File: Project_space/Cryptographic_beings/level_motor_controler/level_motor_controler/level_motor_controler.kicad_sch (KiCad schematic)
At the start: 7 parts, among them J1 Conn_01x15, J2 Conn_01x15, J3 Conn_01x04, J4 Conn_02x03_Odd_Even, J5 Conn_02x03_Odd_Even, J6 Conn_01x02

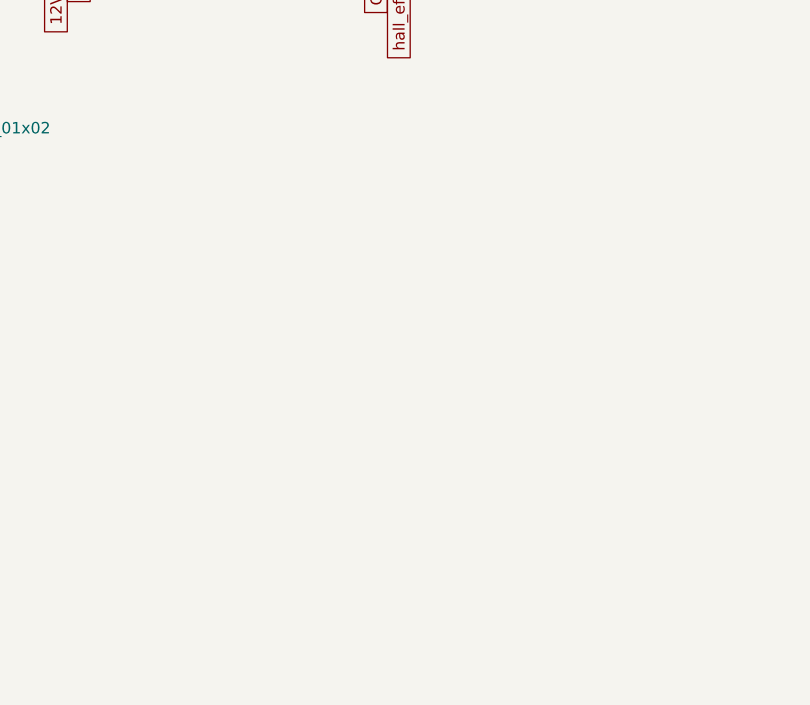
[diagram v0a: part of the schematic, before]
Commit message: Fix Nano pin mapping: swap STEP/DIR to match actual wiring (D4=DIR, D5=STP, D3=HALL)
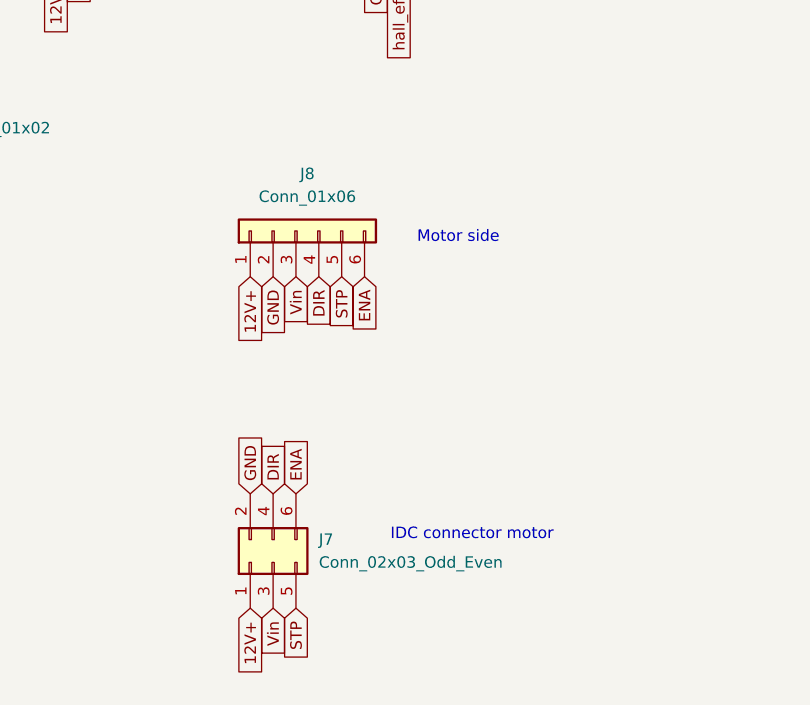
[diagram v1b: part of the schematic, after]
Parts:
- added J7: Conn_02x03_Odd_Even, symbol Connector_Generic:Conn_02x03_Odd_Even
- added J8: Conn_01x06, symbol Connector_Generic:Conn_01x06
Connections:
- net 12V+: now also J7.1 (Pin_1), J8.1 (Pin_1)
- net GND: now also J7.2 (Pin_2), J8.2 (Pin_2)
- net Vin: now also J7.3 (Pin_3), J8.3 (Pin_3)
- new net DIR: J7.4 (Pin_4), J8.4 (Pin_4)
- new net ENA: J7.6 (Pin_6), J8.6 (Pin_6)
- new net STP: J7.5 (Pin_5), J8.5 (Pin_5)
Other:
- note added: "IDC connector motor"
- note added: "Motor side"
